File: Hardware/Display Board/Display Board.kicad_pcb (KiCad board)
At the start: 2 copper layers, 165.1 x 88.9 mm, 44 parts, among them J1 GPS, J10 Conn_02x03_Odd_Even, J11 Conn_02x03_Odd_Even, J12 Conn_02x03_Odd_Even, J13 Conn_02x03_Odd_Even, J14 Conn_02x03_Odd_Even, J15 Conn_02x03_Odd_Even, J16 Conn_02x03_Odd_Even, J17 Conn_02x03_Odd_Even, J18 Conn_02x03_Odd_Even, J19 Conn_02x03_Odd_Even, J2 RTC, J20 Conn_02x03_Odd_Even, J21 Conn_02x03_Odd_Even, J22 Conn_02x03_Odd_Even, J23 Conn_02x03_Odd_Even, J24 Conn_02x03_Odd_Even, J25 Conn_02x03_Odd_Even, J26 Conn_02x03_Odd_Even, J27 Conn_02x03_Odd_Even, J28 Conn_02x03_Odd_Even, J29 Conn_02x03_Odd_Even, J3 CONTROLLER, J30 Conn_02x03_Odd_Even, J31 Conn_02x03_Odd_Even, J4 H:M, J5 M:D, J6 M:S, J7 D:Y, J8 Conn_02x03_Odd_Even, J9 Conn_02x03_Odd_Even

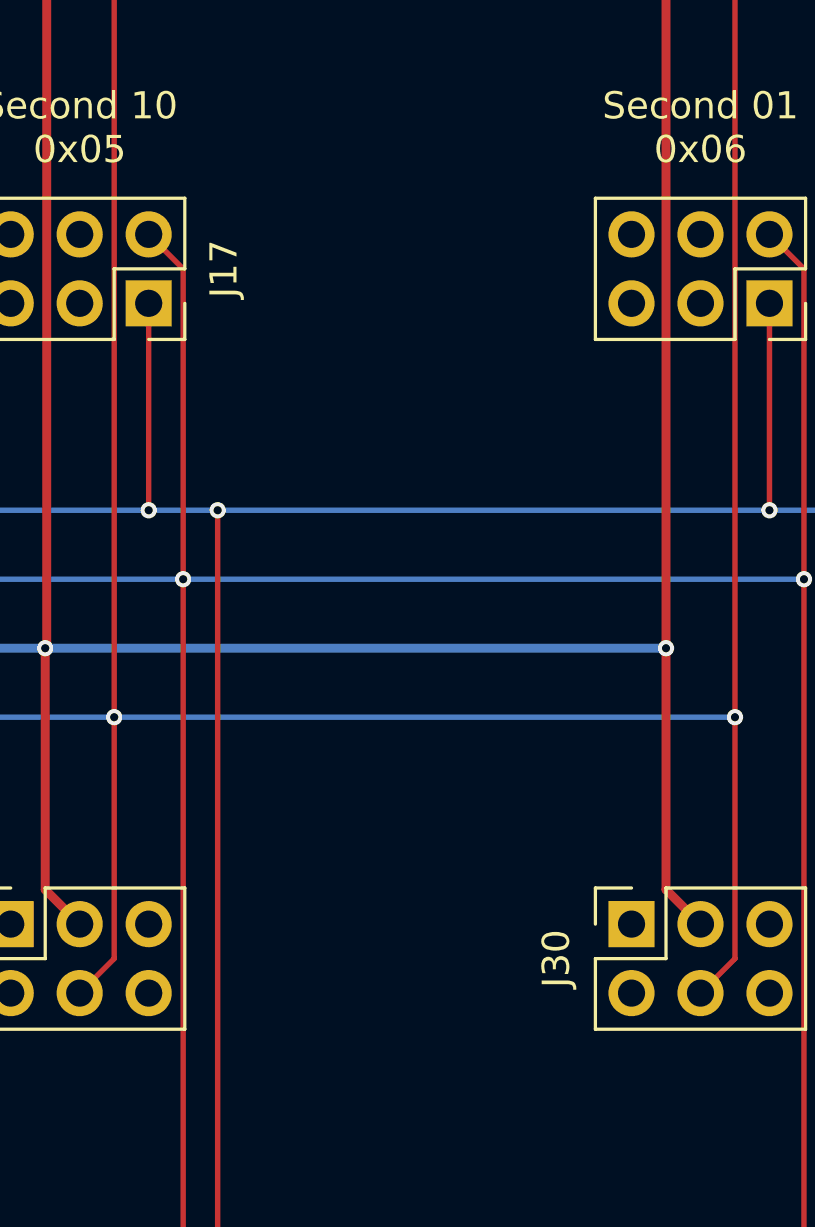
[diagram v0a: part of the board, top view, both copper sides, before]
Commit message: Added holes for the antenna holder
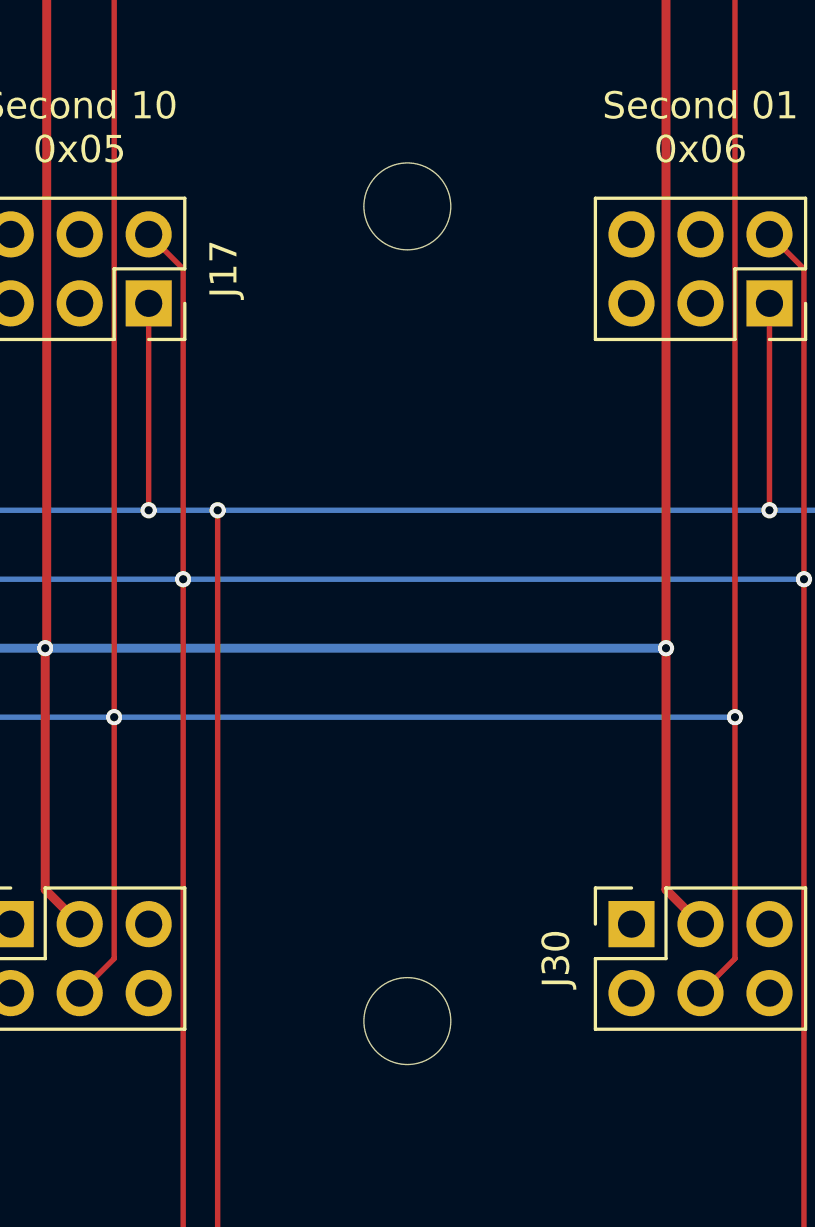
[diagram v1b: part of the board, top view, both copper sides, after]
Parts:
- added AE1: Antenna, DisplayBoard:GPS Antenna Holder, B.Cu at (193.7, 108.0)
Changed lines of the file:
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@@
+		)
+	)
+	(footprint "DisplayBoard:GPS Antenna Holder"
+		(layer "B.Cu")
+		(at 193.675 107.95 180)
+		(property "Reference" "AE1"
+			(at 0 0.5 0)
+			(unlocked yes)
+			(layer "B.SilkS")
+			(effects
+				(font
+					(size 1 1)
+					(thickness 0.1)
+				)
+				(justify mirror)
+			)
+		)
+		(property "Value" "Antenna"
+			(at 0 -1 0)
+			(unlocked yes)
+			(layer "B.Fab")
+			(effects
+				(font
+					(size 1 1)
+					(thickness 0.15)
+				)
+				(justify mirror)
+			)
+		)
+		(property "Footprint" "DisplayBoard:GPS Antenna Holder"
+			(at 0 0 0)
+			(unlocked yes)
+			(layer "B.Fab")
+			(hide yes)
+			(effects
+				(font
+					(size 1 1)
+					(thickness 0.15)
+				)
+				(justify mirror)
+			)
+		)
+		(property "Datasheet" ""
+			(at 0 0 0)
+			(unlocked yes)
+			(layer "B.Fab")
+			(hide yes)
+			(effects
+				(font
+					(size 1 1)
+					(thickness 0.15)
+				)
+				(justify mirror)
+			)
+		)
+		(property "Description" "Antenna"
+			(at 0 0 0)
+			(unlocked yes)
+			(layer "B.Fab")
+			(hide yes)
+			(effects
+				(font
+					(size 1 1)
+					(thickness 0.15)
+				)
+				(justify mirror)
+			)
+		)
+		(sheetname "Root")
+		(sheetfile "Display Board.kicad_sch")
+		(fp_rect
+			(start -12 20)
+			(end 12 -20)
+			(stroke
+				(width 0.05)
+				(type default)
+			)
+			(fill none)
+			(layer "B.CrtYd")
+		)
+		(fp_rect
+			(start -16 9)
+			(end 16 -9)
+			(stroke
+				(width 0.05)
+				(type default)
+			)
+			(fill none)
+			(layer "B.CrtYd")
+		)
+		(fp_circle
+			(center 0 15)
+			(end 3.5 15)
+			(stroke
+				(width 0.1)
+				(type default)
+			)
+			(fill none)
+			(layer "F.CrtYd")
+		)
+		(fp_circle
+			(center 0 -15)
+			(end 3.5 -15)
+			(stroke
+				(width 0.1)
+				(type default)
+			)
+			(fill none)
+			(layer "F.CrtYd")
+		)
+		(fp_rect
+			(start -16 -16.5)
+			(end 16 16.5)
+			(stroke
+				(width 0.1)
+				(type default)
+			)
+			(fill none)
+			(layer "B.Fab")
+		)
+		(fp_text user "${REFERENCE}"
+			(at 0 -2.5 0)
+			(unlocked yes)
+			(layer "B.Fab")
+			(effects
+				(font
+					(size 1 1)
+					(thickness 0.15)
+				)
+				(justify mirror)
+			)
+		)
+		(pad "" np_thru_hole circle
+			(at 0 -15 180)
+			(size 3.2 3.2)
+			(drill 3.2)
+			(layers "*.Mask")
+		)
+		(pad "" np_thru_hole circle
+			(at 0 15 180)
+			(size 3.2 3.2)
+			(drill 3.2)
+			(layers "*.Mask")
+		)
+		(model "C:/Users/aaron/MPLABXProjects/NixieClock/Hardware/3D/GPS Antenna Holder.step"
+			(offset
+				(xyz 15 0 2)
+			)
+			(scale
+				(xyz 1 1 1)
+			)
+			(rotate
+				(xyz -90 0 90)
+			)
 		)
 	)

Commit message: Added JLCPCB order number placeholder.
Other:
- board text added: "JLCJLCJLCJLC"
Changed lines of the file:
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@@
+		)
+	)
+	(gr_text "JLCJLCJLCJLC"
+		(at 139.7 151.13 0)
+		(layer "F.SilkS")
+		(effects
+			(font
+				(size 1 1)
+				(thickness 0.2)
+				(bold yes)
+			)
+			(justify bottom)
 		)
 	)

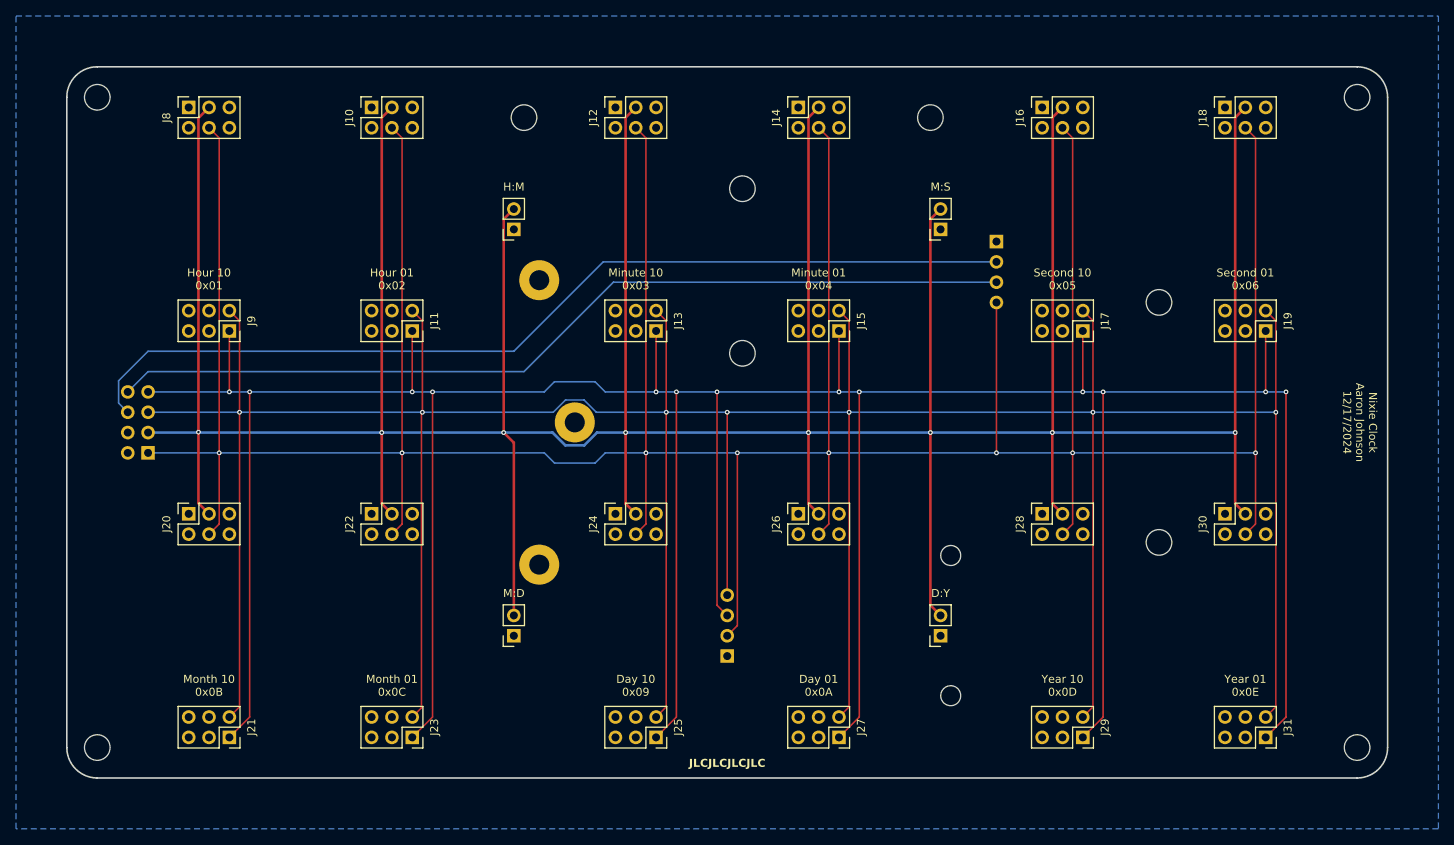
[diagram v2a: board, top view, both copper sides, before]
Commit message: Updated Display Board to V2 Nixies
The Antenna holder needs to be redesigned. Lots of silkscreen errors to fix.
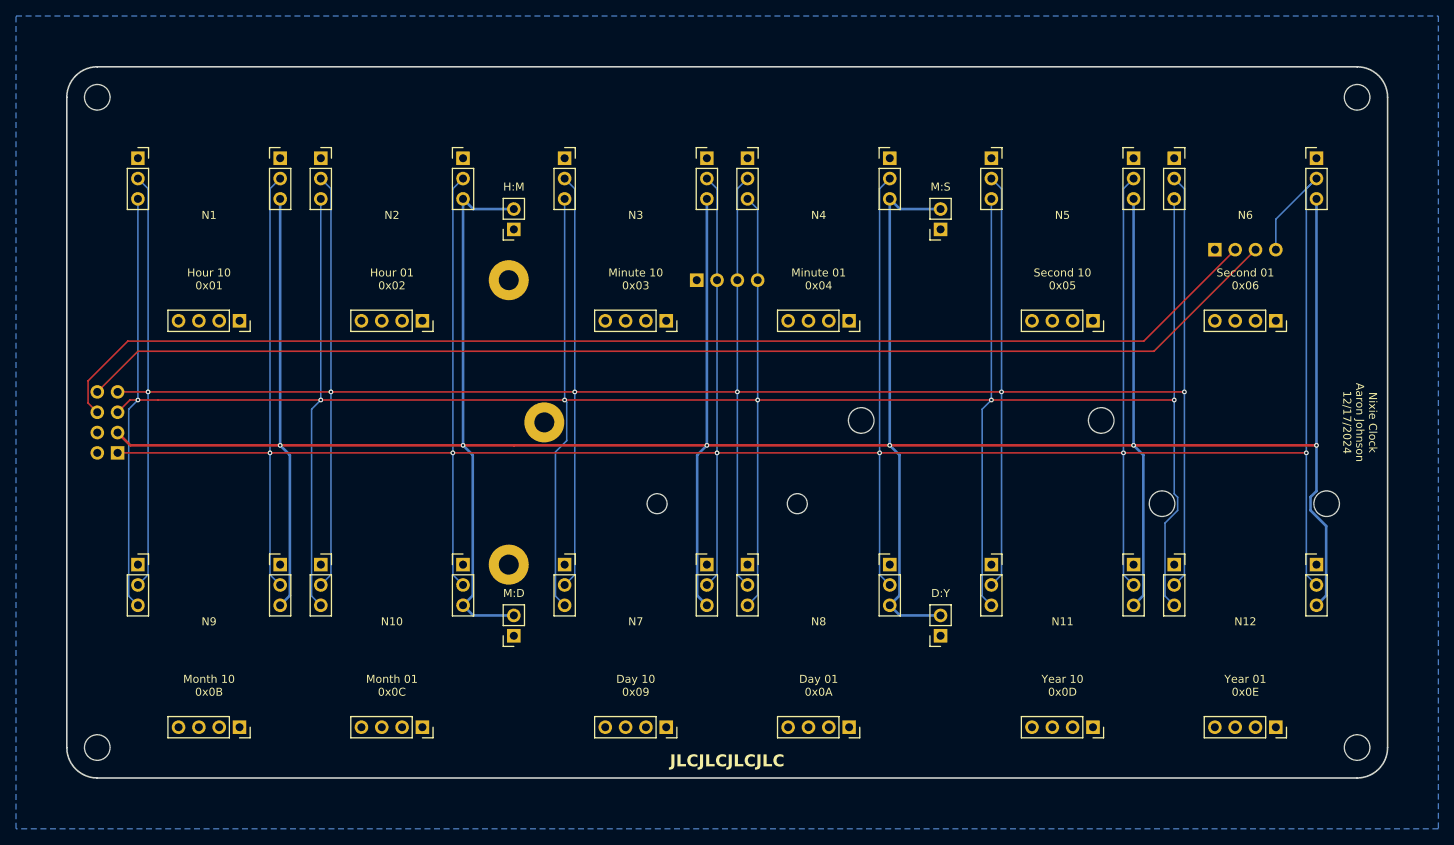
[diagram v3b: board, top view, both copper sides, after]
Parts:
- removed H12, H13: MountingHole, MountingHole:MountingHole_3.2mm_M3
- removed J10, J11, J12, J13, J14, J15, J16, J17, J18, J19, J20, J21, J22, J23, J24, J25, J26, J27, J28, J29, J30, J31, J8, J9: Conn_02x03_Odd_Even, Connector_PinSocket_2.54mm:PinSocket_2x03_P2.54mm_Vertical
- added N1: ~, Nixie:Nixie Driver V2, F.Cu at (74.9, 82.5)
- added N10: ~, Nixie:Nixie Driver V2, F.Cu at (97.8, 133.3)
- added N11: ~, Nixie:Nixie Driver V2, F.Cu at (181.6, 133.3)
- added N12: ~, Nixie:Nixie Driver V2, F.Cu at (204.5, 133.3)
- added N2: ~, Nixie:Nixie Driver V2, F.Cu at (97.8, 82.5)
- added N3: ~, Nixie:Nixie Driver V2, F.Cu at (128.3, 82.5)
- added N4: ~, Nixie:Nixie Driver V2, F.Cu at (151.1, 82.5)
- added N5: ~, Nixie:Nixie Driver V2, F.Cu at (181.6, 82.5)
- added N6: ~, Nixie:Nixie Driver V2, F.Cu at (204.5, 82.5)
- added N7: ~, Nixie:Nixie Driver V2, F.Cu at (128.3, 133.3)
- added N8: ~, Nixie:Nixie Driver V2, F.Cu at (151.1, 133.3)
- added N9: ~, Nixie:Nixie Driver V2, F.Cu at (74.9, 133.3)
- AE1: value Antenna -> GPS
- moved H3 75.4 mm to (214.6, 118.1), turned to -90 degrees
- moved H6 65.6 mm to (194.1, 118.1), turned to -90 degrees
- moved J2 47.1 mm to (135.9, 90.2), turned to -90 degrees
- moved H5 43.9 mm to (130.9, 118.1), turned to -90 degrees
- moved J1 27.3 mm to (200.7, 86.4), turned to -90 degrees
- moved AE1 22.2 mm to (171.4, 107.7), turned to -90 degrees
- moved H2 20.2 mm to (148.5, 118.1), turned to -90 degrees
- moved H1 3.81 mm to (112.4, 90.2)
- moved H4 3.81 mm to (116.8, 108.0)
- moved H7 3.81 mm to (112.4, 125.7)
- moved J3 3.81 mm to (63.5, 111.8)
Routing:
- net Vnn: track 552.2 -> 489.5 mm, vias 8 -> 6
- net SDA: track 482.9 -> 444.5 mm, vias 13 -> 6
- net MCU TX / GPS RX: track 114.3 -> 152.1 mm
- net MCU RX / GPS TX: track 120.3 -> 154.6 mm
- net SCL: track 476.2 -> 443.9 mm, vias 7 -> 6
- net Vdd: track 492.8 -> 470.7 mm, vias 8 -> 6
